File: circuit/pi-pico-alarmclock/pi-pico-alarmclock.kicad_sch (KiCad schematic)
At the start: 33 parts, among them J1 Screw_Terminal_2_P5.00mm, J2 BTN GREEN, J3 BTN BLUE, J4 BTN_YELLOW, J5 NEOPIXEL, J6 OLED, J7 BAT - Screw_Terminal_2_P5.00mm, Q1 IRLZ44N, Q3 IRF9540, Q4 IRLZ44N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

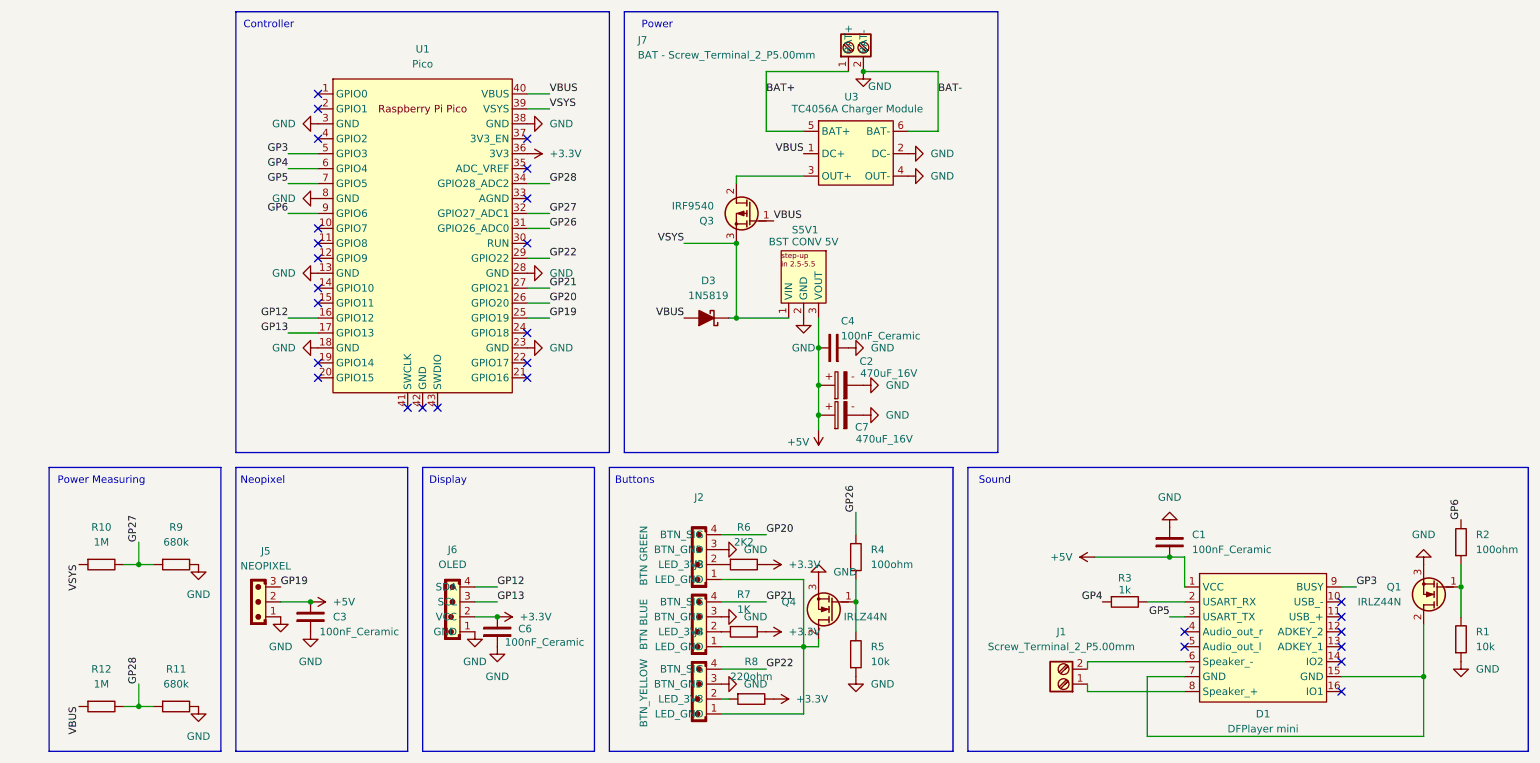
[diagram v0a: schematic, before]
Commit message: Move Neopixel control pin from GPIO19 to GPIO15, introduce power management for Neopixel via GPIO14 and another IRLZ44N.
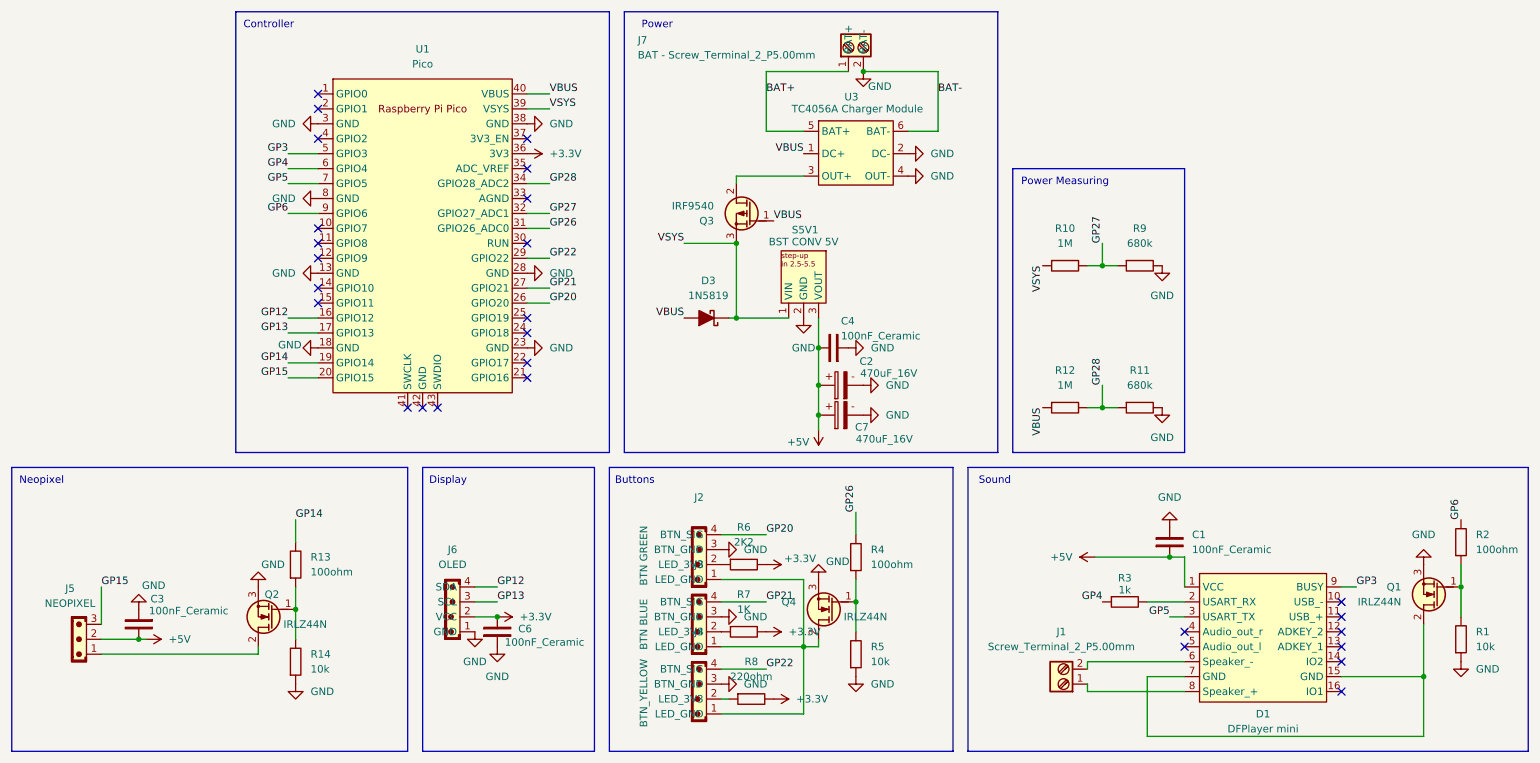
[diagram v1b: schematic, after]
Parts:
- added Q2: IRLZ44N, PCM_Package_TO_SOT_THT_AKL:TO-220-3_Vertical_GDS, symbol PCM_Transistor_MOSFET_AKL:IRLZ44N
- added R13: 100ohm, Resistor_THT:R_Axial_DIN0207_L6.3mm_D2.5mm_P10.16mm_Horizontal, symbol PCM_SL_Resistors:100ohm
- added R14: 10k, Resistor_THT:R_Axial_DIN0207_L6.3mm_D2.5mm_P10.16mm_Horizontal, symbol PCM_SL_Resistors:10k
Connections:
- net GND: now also Q2.3 (S), R14.1; no longer J5.1
- net GP14: now reaches U1.19 (GPIO14)
- net GP14: now also R13.2
- net GP15: now reaches U1.20 (GPIO15)
- net GP15: now also J5.3
- net GP19: no longer names the net of U1.25 (GPIO19)
- net GP19: no longer J5.3
- new net: J5.1, Q2.2 (D)
- new net: Q2.1 (G), R13.1, R14.2
- no-connect marks 28 -> 27
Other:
- moved on the sheet: C3, J5, R10, R11, R12, R9

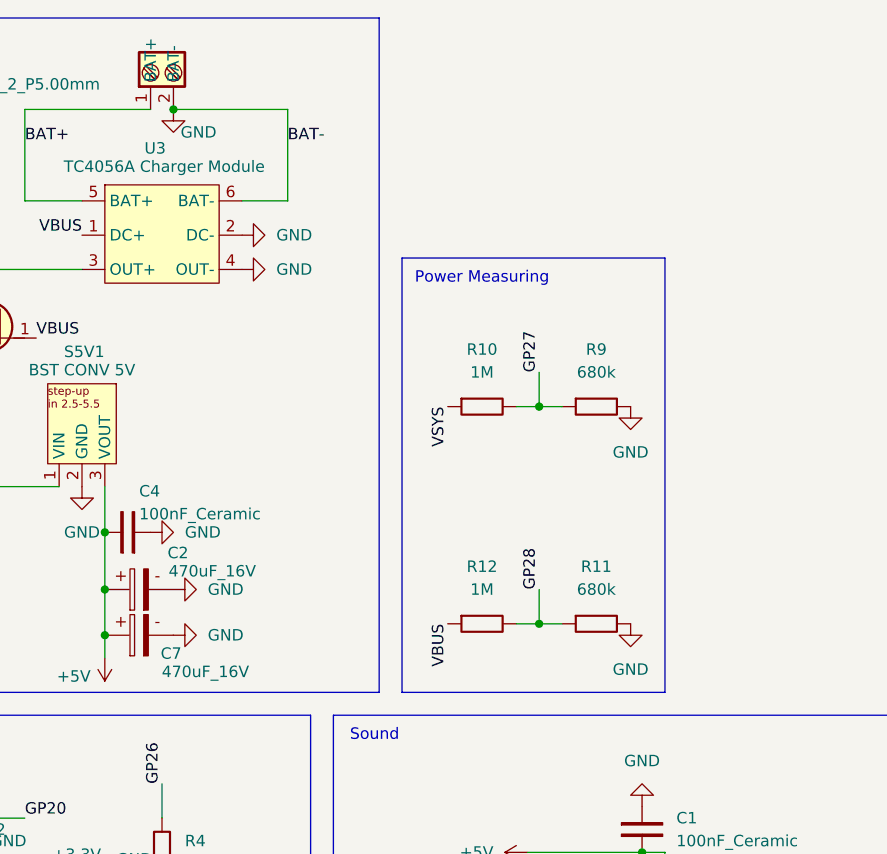
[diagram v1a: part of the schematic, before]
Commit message: Correct GPIO nets, update placements and values
Rename GPIO nets (GP14/GP15/GP19) and Q2 nets; adjust pad pintypes.
Reposition multiple footprints and update silk/fab layers. Change
resistor values (1M -> 200K, 680k -> 100K). Add PCB .stl step file, plus
GND symbols and a 100nF decoupling cap.
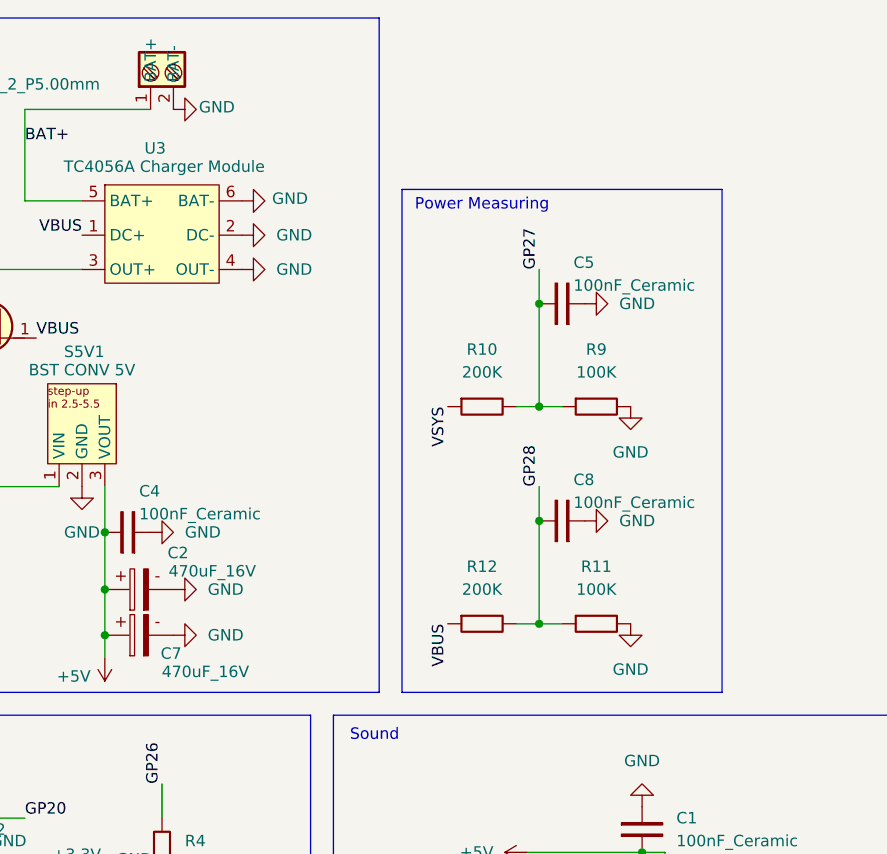
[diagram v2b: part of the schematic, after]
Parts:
- added C5, C8: 100nF_Ceramic, Capacitor_THT:C_Disc_D5.0mm_W2.5mm_P2.50mm, symbol PCM_SL_Capacitors:100nF_Ceramic
- R10, R12: value 1M -> 200K
- R11, R9: value 680k -> 100K
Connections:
- net GND: now also C5.1, C8.1
- net GP27: now also C5.2
- net GP28: now also C8.2
